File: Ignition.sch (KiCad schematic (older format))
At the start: 10 parts, among them Q1 Q_PMOS_GDS, Q2 Q_PMOS_GDS, Q3 Q_PMOS_GDS

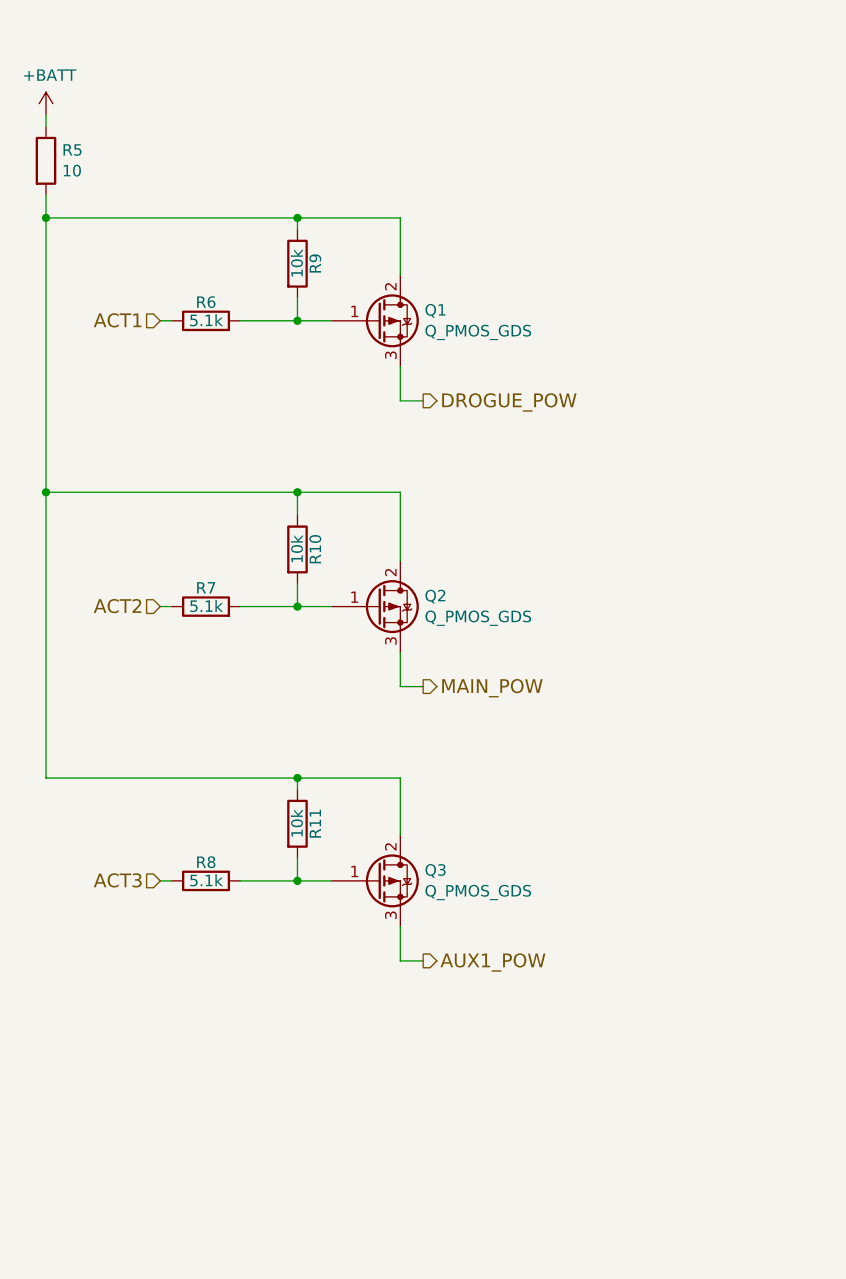
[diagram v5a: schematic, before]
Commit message: Fixed .gitmodules (host-agnostic) Added bypass caps Added NMOS to ignition sheet Added current-limiting resistors Fixed 3V3 ADC input
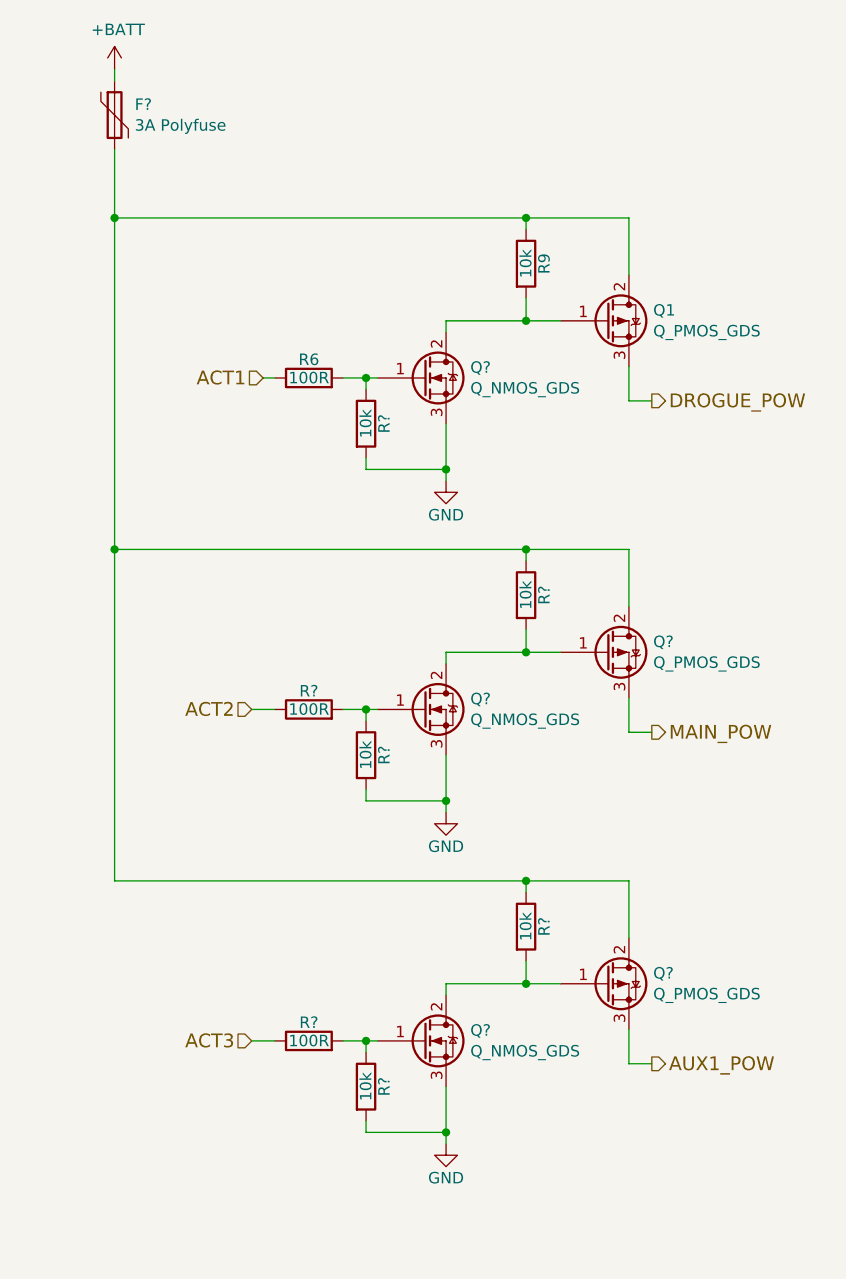
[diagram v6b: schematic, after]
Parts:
- removed Q2, Q3: Q_PMOS_GDS, Package_TO_SOT_SMD:SOT-23, symbol Device:Q_PMOS_GDS
- removed R10, R11: 10k, Resistor_SMD:R_1206_3216Metric_Pad1.42x1.75mm_HandSolder, symbol Device:R
- removed R5: 10, TerminalBlock:TerminalBlock_bornier-2_P5.08mm, symbol Device:R
- removed R7, R8: 5.1k, Resistor_SMD:R_1206_3216Metric_Pad1.42x1.75mm_HandSolder, symbol Device:R
- added F?: 3A Polyfuse, Resistor_SMD:R_1206_3216Metric_Pad1.42x1.75mm_HandSolder, symbol Device:Polyfuse
- added Q? (x2): Q_PMOS_GDS, Package_TO_SOT_SMD:SOT-23, symbol Device:Q_PMOS_GDS
- added Q? (x3): Q_NMOS_GDS, symbol Device:Q_NMOS_GDS
- added R? (x5): 10k, Resistor_SMD:R_1206_3216Metric_Pad1.42x1.75mm_HandSolder, symbol Device:R
- added R? (x2): 100R, Resistor_SMD:R_1206_3216Metric_Pad1.42x1.75mm_HandSolder, symbol Device:R
- R6: value 5.1k -> 100R
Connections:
- net +BATT: now also F?.1
- net ACT2: now also R?.1
- net ACT3: now also R?.1
- net AUX1_POW: now also Q?.3 (S)
- net MAIN_POW: now also Q?.3 (S)
- net at Q1.2 (D), R9.1: now also F?.2, Q?.2 (D), Q?.2 (D), R?.1, R?.1
- net at Q1.1 (G), R9.2: now also Q?.2 (D); no longer R6.2
- new net: Q?.1 (G), R6.2, R?.1
- new net: Q?.1 (G), Q?.2 (D), R?.2 (x2)
- new net: Q?.1 (G), R?.1, R?.2 (x2)
- new net GND: Q?.3 (S), Q?.3 (S), Q?.3 (S), R?.2, R?.2, R?.2
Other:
- moved on the sheet: Q1, R6, R9

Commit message: Add external oscillator Add BOOT0 pulldown Remove NRST external pullup Add test LEDs Smaller JTAG connector
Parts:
- F?: footprint Resistor_SMD:R_1206_3216Metric_Pad1.42x1.75mm_HandSolder -> Fuse:Fuse_1206_3216Metric_Pad1.42x1.75mm_HandSolder
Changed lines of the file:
@@
 F 0 "F?" H 3788 1346 50  0000 L CNN
 F 1 "3A Polyfuse" H 3788 1255 50  0000 L CNN
-F 2 "Resistor_SMD:R_1206_3216Metric_Pad1.42x1.75mm_HandSolder" H 3750 1100 50  0001 L CNN
+F 2 "Fuse:Fuse_1206_3216Metric_Pad1.42x1.75mm_HandSolder" H 3750 1100 50  0001 L CNN
 F 3 "~" H 3700 1300 50  0001 C CNN
 	1    3700 1300

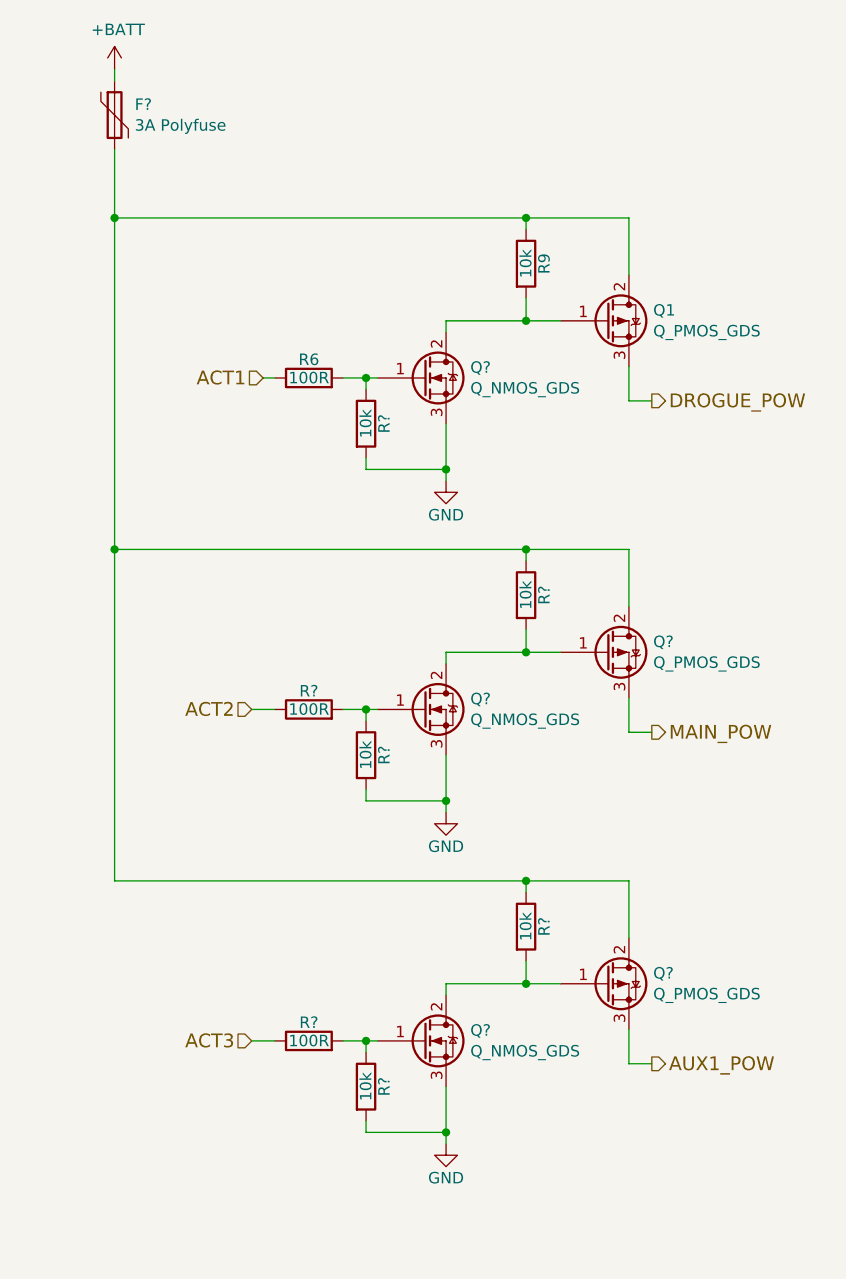
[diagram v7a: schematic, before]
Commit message: Annotated schematic Added 2N7002 packages Updated PCB
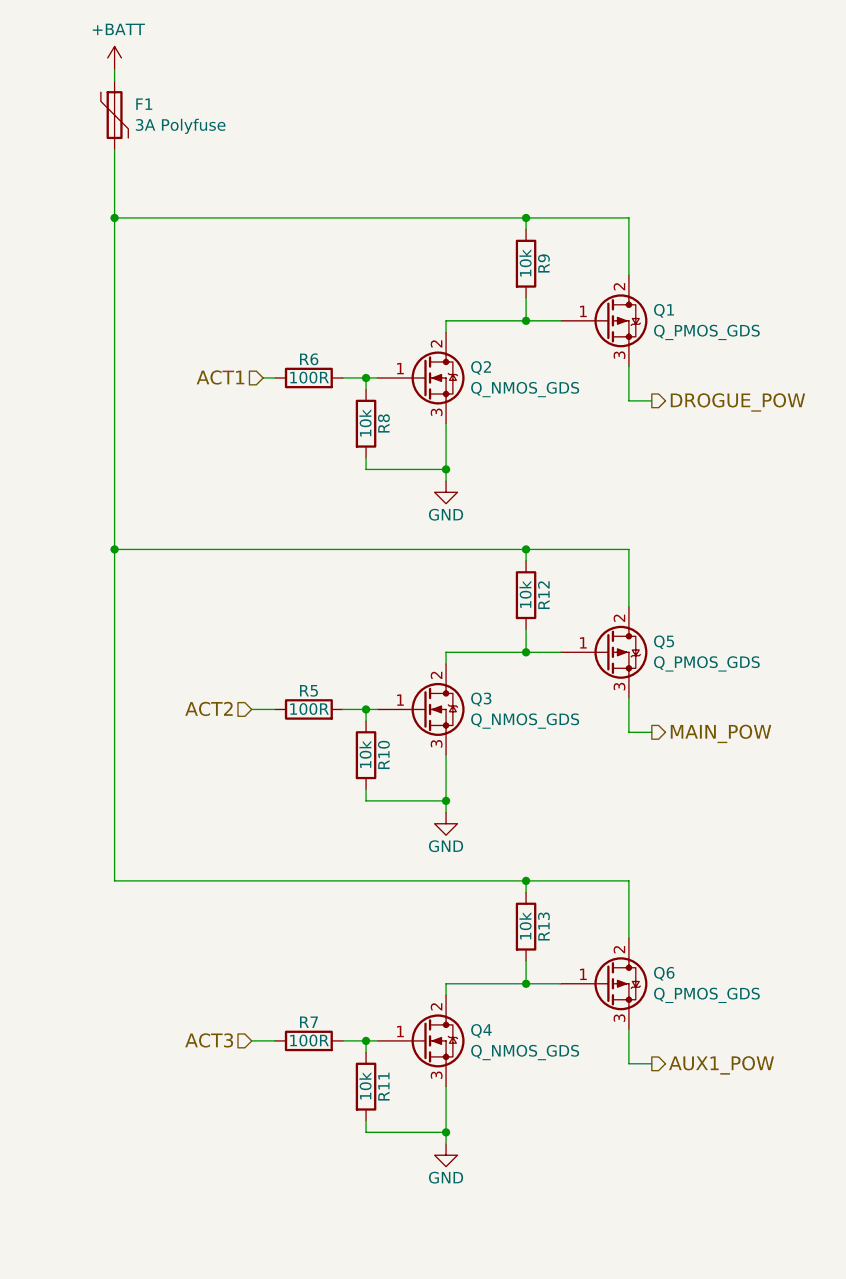
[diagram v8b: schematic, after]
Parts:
- Q2, Q3, Q4: renamed from Q?; footprint (none) -> Package_TO_SOT_SMD:SOT-23
- gave numbers to parts that had none: 10
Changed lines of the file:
@@
 	3700 1450 3700 1750
 $Comp
-L Device:Q_NMOS_GDS Q?
+L Device:Q_NMOS_GDS Q2
 U 1 1 5ED9D4A9
 P 5050 2450
-F 0 "Q?" H 5256 2496 50  0000 L CNN
+F 0 "Q2" H 5256 2496 50  0000 L CNN
 F 1 "Q_NMOS_GDS" H 5256 2405 50  0000 L CNN
-F 2 "" H 5250 2550 50  0001 C CNN
+F 2 "Package_TO_SOT_SMD:SOT-23" H 5250 2550 50  0001 C CNN
 F 3 "~" H 5050 2450 50  0001 C CNN
 	1    5050 2450
@@
 $EndComp
 $Comp
-L Device:Polyfuse F?
+L Device:Polyfuse F1
 U 1 1 5EDBA400
 P 3700 1300
-F 0 "F?" H 3788 1346 50  0000 L CNN
+F 0 "F1" H 3788 1346 50  0000 L CNN
 F 1 "3A Polyfuse" H 3788 1255 50  0000 L CNN
 F 2 "Fuse:Fuse_1206_3216Metric_Pad1.42x1.75mm_HandSolder" H 3750 1100 50  0001 L CNN
@@
 P 5150 2900
 AR Path="/5E4AF051" Ref="#PWR?"  Part="1"
-AR Path="/5AB1811C/5E4AF051" Ref="#PWR?"  Part="1"
-F 0 "#PWR?" H 5150 2650 50  0001 C CNN
+AR Path="/5AB1811C/5E4AF051" Ref="#PWR0105"  Part="1"
+F 0 "#PWR0105" H 5150 2650 50  0001 C CNN
 F 1 "GND" H 5150 2750 50  0000 C CNN
 F 2 "" H 5150 2900 50  0001 C CNN
@@
 	4700 2450 4800 2450
 $Comp
-L Device:R R?
+L Device:R R8
 U 1 1 5E4B3E1D
 P 4800 2650
-F 0 "R?" V 4880 2650 50  0000 C CNN
+F 0 "R8" V 4880 2650 50  0000 C CNN
 F 1 "10k" V 4800 2650 50  0000 C CNN
 F 2 "Resistor_SMD:R_1206_3216Metric_Pad1.42x1.75mm_HandSolder" V 4730 2650 50  0001 C CNN
@@
 	4800 2450 4850 2450
 $Comp
-L Device:R R?
+L Device:R R12
 U 1 1 5E4C3E0F
 P 5500 3400
-F 0 "R?" V 5580 3400 50  0000 C CNN
+F 0 "R12" V 5580 3400 50  0000 C CNN
 F 1 "10k" V 5500 3400 50  0000 C CNN
 F 2 "Resistor_SMD:R_1206_3216Metric_Pad1.42x1.75mm_HandSolder" V 5430 3400 50  0001 C CNN
@@
 $EndComp
 $Comp
-L Device:Q_PMOS_GDS Q?
+L Device:Q_PMOS_GDS Q5
 U 1 1 5E4C3E16
 P 5850 3650
-F 0 "Q?" H 6056 3696 50  0000 L CNN
+F 0 "Q5" H 6056 3696 50  0000 L CNN
 F 1 "Q_PMOS_GDS" H 6056 3605 50  0000 L CNN
 F 2 "Package_TO_SOT_SMD:SOT-23" H 6050 3750 50  0001 C CNN
@@
 	5950 4000 5950 3850
 $Comp
-L Device:R R?
+L Device:R R5
 U 1 1 5E4C3E26
 P 4550 3900
-F 0 "R?" V 4630 3900 50  0000 C CNN
+F 0 "R5" V 4630 3900 50  0000 C CNN
 F 1 "100R" V 4550 3900 50  0000 C CNN
 F 2 "Resistor_SMD:R_1206_3216Metric_Pad1.42x1.75mm_HandSolder" V 4480 3900 50  0001 C CNN
@@
 $EndComp
 $Comp
-L Device:Q_NMOS_GDS Q?
+L Device:Q_NMOS_GDS Q3
 U 1 1 5E4C3E2C
 P 5050 3900
-F 0 "Q?" H 5256 3946 50  0000 L CNN
+F 0 "Q3" H 5256 3946 50  0000 L CNN
 F 1 "Q_NMOS_GDS" H 5256 3855 50  0000 L CNN
-F 2 "" H 5250 4000 50  0001 C CNN
+F 2 "Package_TO_SOT_SMD:SOT-23" H 5250 4000 50  0001 C CNN
 F 3 "~" H 5050 3900 50  0001 C CNN
 	1    5050 3900
@@
 P 5150 4350
 AR Path="/5E4C3E34" Ref="#PWR?"  Part="1"
-AR Path="/5AB1811C/5E4C3E34" Ref="#PWR?"  Part="1"
-F 0 "#PWR?" H 5150 4100 50  0001 C CNN
+AR Path="/5AB1811C/5E4C3E34" Ref="#PWR0106"  Part="1"
+F 0 "#PWR0106" H 5150 4100 50  0001 C CNN
 F 1 "GND" H 5150 4200 50  0000 C CNN
 F 2 "" H 5150 4350 50  0001 C CNN
@@
 $EndComp
 Wire Wire Line
-	5150 4100 5150 4300
-Wire Wire Line
 	4700 3900 4800 3900
 $Comp
-L Device:R R?
+L Device:R R10
 U 1 1 5E4C3E3C
 P 4800 4100
-F 0 "R?" V 4880 4100 50  0000 C CNN
+F 0 "R10" V 4880 4100 50  0000 C CNN
 F 1 "10k" V 4800 4100 50  0000 C CNN
 F 2 "Resistor_SMD:R_1206_3216Metric_Pad1.42x1.75mm_HandSolder" V 4730 4100 50  0001 C CNN
@@
 Wire Wire Line
 	4800 4300 5150 4300
-Connection ~ 5150 4300
-Wire Wire Line
-	5150 4300 5150 4350
 Wire Wire Line
 	4800 3950 4800 3900
@@
 	4300 3900 4400 3900
 $Comp
-L Device:R R?
+L Device:R R13
 U 1 1 5E4D9D1E
 P 5500 4850
-F 0 "R?" V 5580 4850 50  0000 C CNN
+F 0 "R13" V 5580 4850 50  0000 C CNN
 F 1 "10k" V 5500 4850 50  0000 C CNN
 F 2 "Resistor_SMD:R_1206_3216Metric_Pad1.42x1.75mm_HandSolder" V 5430 4850 50  0001 C CNN
@@
 $EndComp
 $Comp
-L Device:Q_PMOS_GDS Q?
+L Device:Q_PMOS_GDS Q6
 U 1 1 5E4D9D25
 P 5850 5100
-F 0 "Q?" H 6056 5146 50  0000 L CNN
+F 0 "Q6" H 6056 5146 50  0000 L CNN
 F 1 "Q_PMOS_GDS" H 6056 5055 50  0000 L CNN
 F 2 "Package_TO_SOT_SMD:SOT-23" H 6050 5200 50  0001 C CNN
@@
 	5950 5450 5950 5300
 $Comp
-L Device:R R?
+L Device:R R7
 U 1 1 5E4D9D34
 P 4550 5350
-F 0 "R?" V 4630 5350 50  0000 C CNN
+F 0 "R7" V 4630 5350 50  0000 C CNN
 F 1 "100R" V 4550 5350 50  0000 C CNN
 F 2 "Resistor_SMD:R_1206_3216Metric_Pad1.42x1.75mm_HandSolder" V 4480 5350 50  0001 C CNN
@@
 $EndComp
 $Comp
-L Device:Q_NMOS_GDS Q?
+L Device:Q_NMOS_GDS Q4
 U 1 1 5E4D9D3A
 P 5050 5350
-F 0 "Q?" H 5256 5396 50  0000 L CNN
+F 0 "Q4" H 5256 5396 50  0000 L CNN
 F 1 "Q_NMOS_GDS" H 5256 5305 50  0000 L CNN
-F 2 "" H 5250 5450 50  0001 C CNN
+F 2 "Package_TO_SOT_SMD:SOT-23" H 5250 5450 50  0001 C CNN
 F 3 "~" H 5050 5350 50  0001 C CNN
 	1    5050 5350
@@
 P 5150 5800
 AR Path="/5E4D9D42" Ref="#PWR?"  Part="1"
-AR Path="/5AB1811C/5E4D9D42" Ref="#PWR?"  Part="1"
-F 0 "#PWR?" H 5150 5550 50  0001 C CNN
+AR Path="/5AB1811C/5E4D9D42" Ref="#PWR0107"  Part="1"
+F 0 "#PWR0107" H 5150 5550 50  0001 C CNN
 F 1 "GND" H 5150 5650 50  0000 C CNN
 F 2 "" H 5150 5800 50  0001 C CNN
@@
 	4700 5350 4800 5350
 $Comp
-L Device:R R?
+L Device:R R11
 U 1 1 5E4D9D4A
 P 4800 5550
-F 0 "R?" V 4880 5550 50  0000 C CNN
+F 0 "R11" V 4880 5550 50  0000 C CNN
 F 1 "10k" V 4800 5550 50  0000 C CNN
 F 2 "Resistor_SMD:R_1206_3216Metric_Pad1.42x1.75mm_HandSolder" V 4730 5550 50  0001 C CNN
@@
 Wire Wire Line
 	3700 3200 3700 4650
+Wire Wire Line
+	5150 4100 5150 4300
+Connection ~ 5150 4300
+Wire Wire Line
+	5150 4300 5150 4350
 $EndSCHEMATC
